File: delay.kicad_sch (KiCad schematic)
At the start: 50 parts, among them U1 L7805, U2 TL072, U3 PT2399

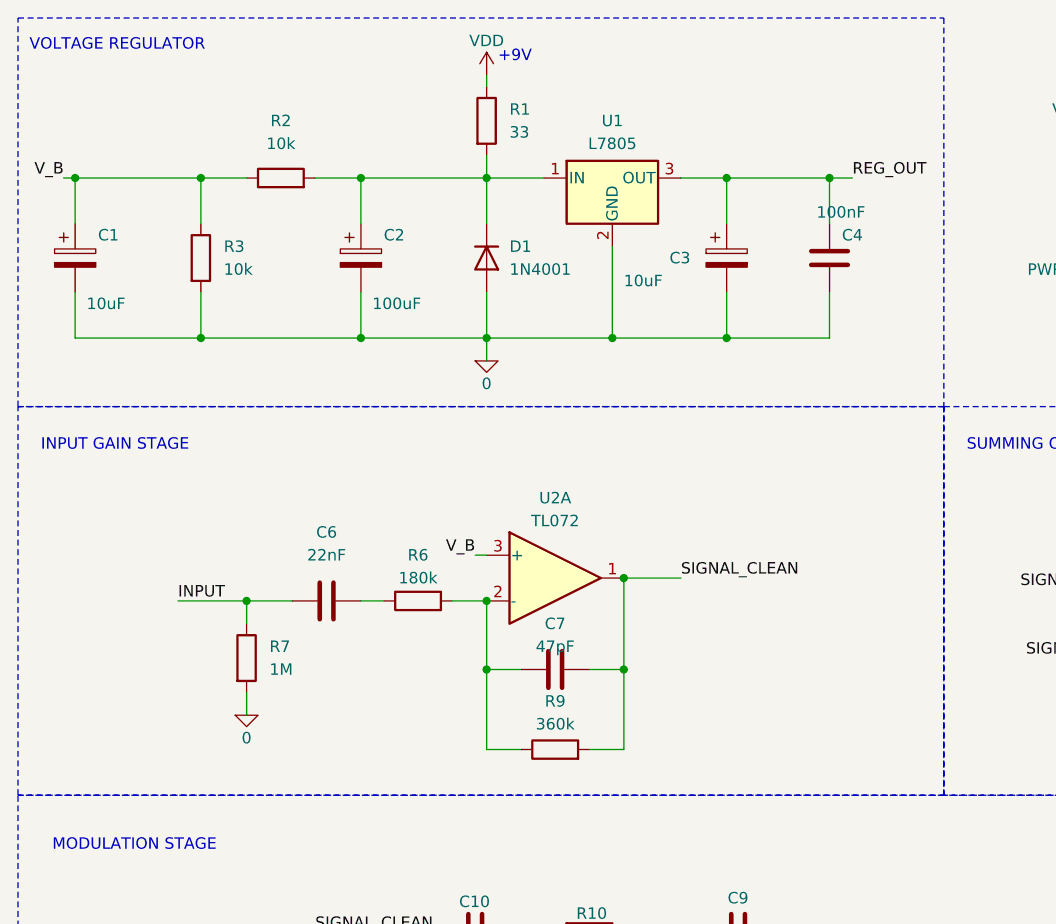
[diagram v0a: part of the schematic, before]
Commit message: add footprint for each element
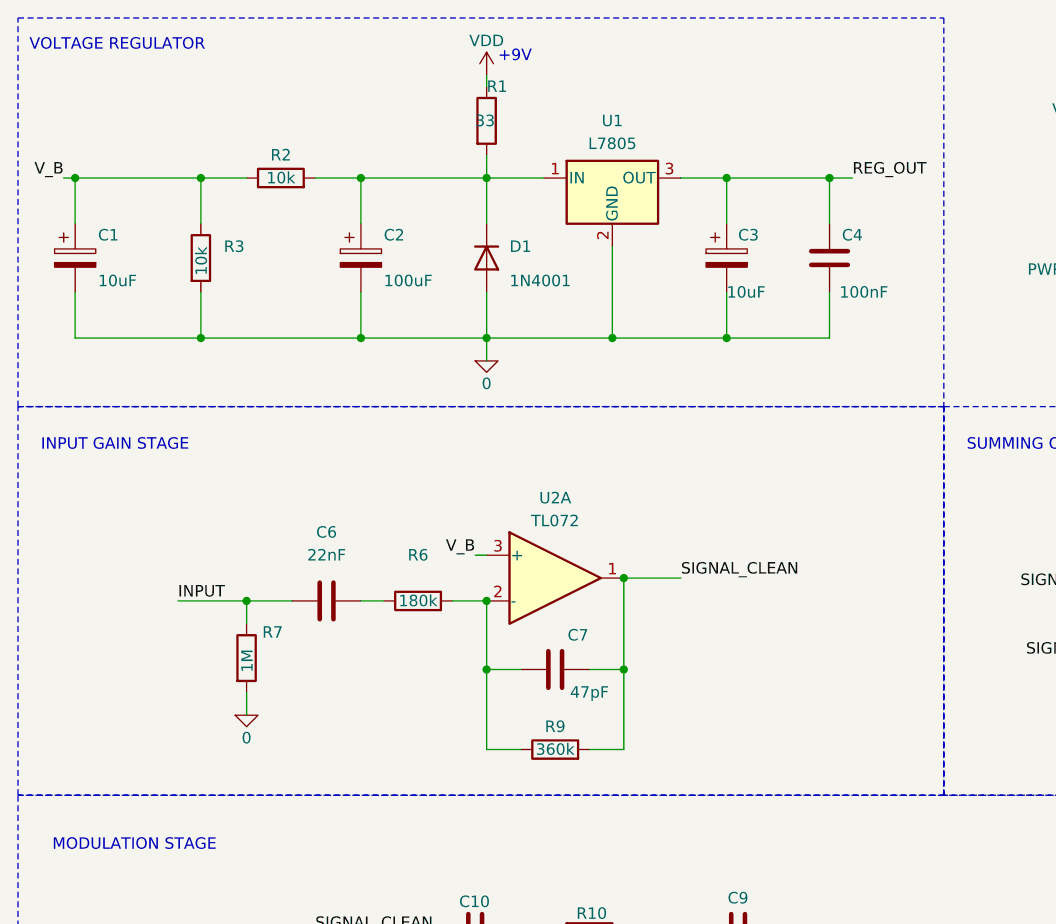
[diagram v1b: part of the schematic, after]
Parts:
- C1, C13, C2, C3: footprint (none) -> Capacitor_SMD:CP_Elec_8x10
- C10, C11, C12, C14, C15, C16, C17, C18, C19, C20, C21, C22, C23, C4, C5, C6, C7, C8, C9: footprint (none) -> Capacitor_SMD:C_0805_2012Metric_Pad1.18x1.45mm_HandSolder
- DELAY1, FDBK1, MIX1: footprint (none) -> Potentiometer_THT:Potentiometer_Alps_RK163_Single_Horizontal
- R1, R10, R11, R12, R13, R14, R15, R16, R17, R18, R19, R2, R20, R3, R4, R5, R6, R7, R8, R9: footprint (none) -> Resistor_SMD:R_0805_2012Metric_Pad1.20x1.40mm_HandSolder
- U1: footprint (none) -> Regulators:TO255P1020X450X2000-3
- U2: footprint (none) -> Op-Amps:DIP794W45P254L1060H508Q8

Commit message: add list of components and respective links, add real footprints
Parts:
- C1, C3: footprint Capacitor_SMD:CP_Elec_8x10 -> Capacitor:EEE1AA220WR
- C13, C2: footprint Capacitor_SMD:CP_Elec_8x10 -> Capacitor:EEE1AA101SP
- D1: footprint Diode_THT:D_DO-41_SOD81_P10.16mm_Horizontal -> Diodes:DIOM5226X240N
- U1: footprint Regulators:TO255P1020X450X2000-3 -> Ic:TO255P460X1020X2008-3P
- U2: footprint Op-Amps:DIP794W45P254L1060H508Q8 -> Ic:SOT65P280X110-8N
- U3: footprint Package_DIP:DIP-16_W7.62mm -> Package_SO:SOIC-16_3.9x9.9mm_P1.27mm
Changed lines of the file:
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@@
       (effects (font (size 1.27 1.27)) (justify left))
     )
-    (property "Footprint" "Capacitor_SMD:CP_Elec_8x10" (at 96.2152 44.45 0)
+    (property "Footprint" "Capacitor:EEE1AA220WR" (at 96.2152 44.45 0)
       (effects (font (size 1.27 1.27)) hide)
     )
@@
       (effects (font (size 1.27 1.27)))
     )
-    (property "Footprint" "Regulators:TO255P1020X450X2000-3" (at 83.185 35.56 0)
+    (property "Footprint" "Ic:TO255P460X1020X2008-3P" (at 83.185 35.56 0)
       (effects (font (size 1.27 1.27) italic) (justify left) hide)
     )
@@
       (effects (font (size 1.27 1.27)) (justify right))
     )
-    (property "Footprint" "Package_DIP:DIP-16_W7.62mm" (at 54.61 152.4 0)
+    (property "Footprint" "Package_SO:SOIC-16_3.9x9.9mm_P1.27mm" (at 54.61 152.4 0)
       (effects (font (size 1.27 1.27)) hide)
     )
@@
       (effects (font (size 1.27 1.27)))
     )
-    (property "Footprint" "Op-Amps:DIP794W45P254L1060H508Q8" (at 167.64 74.93 0)
+    (property "Footprint" "Ic:SOT65P280X110-8N" (at 167.64 74.93 0)
       (effects (font (size 1.27 1.27)) hide)
     )
@@
       (effects (font (size 1.27 1.27)) (justify left))
     )
-    (property "Footprint" "Diode_THT:D_DO-41_SOD81_P10.16mm_Horizontal" (at 68.58 40.64 0)
+    (property "Footprint" "Diodes:DIOM5226X240N" (at 68.58 40.64 0)
       (effects (font (size 1.27 1.27)) hide)
     )
@@
       (effects (font (size 1.27 1.27)))
     )
-    (property "Footprint" "Op-Amps:DIP794W45P254L1060H508Q8" (at 76.2 76.2 0)
+    (property "Footprint" "Ic:SOT65P280X110-8N" (at 76.2 76.2 0)
       (effects (font (size 1.27 1.27)) hide)
     )
@@
       (effects (font (size 1.27 1.27)) (justify left))
     )
-    (property "Footprint" "Capacitor_SMD:CP_Elec_8x10" (at 23.8252 44.45 0)
+    (property "Footprint" "Capacitor:EEE1AA220WR" (at 23.8252 44.45 0)
       (effects (font (size 1.27 1.27)) hide)
     )
@@
       (effects (font (size 1.27 1.27)) (justify left))
     )
-    (property "Footprint" "Capacitor_SMD:CP_Elec_8x10" (at 31.75 130.5052 0)
+    (property "Footprint" "Capacitor:EEE1AA101SP" (at 31.75 130.5052 0)
       (effects (font (size 1.27 1.27)) hide)
     )
@@
       (effects (font (size 1.27 1.27)) (justify left))
     )
-    (property "Footprint" "Capacitor_SMD:CP_Elec_8x10" (at 55.5752 44.45 0)
-      (effects (font (size 1.27 1.27)) hide)
-    )
+    (property "Footprint" "Capacitor:EEE1AA101SP" (at 55.5752 44.45 0)
+      (effects (font (size 1.27 1.27)) hide)
+    )

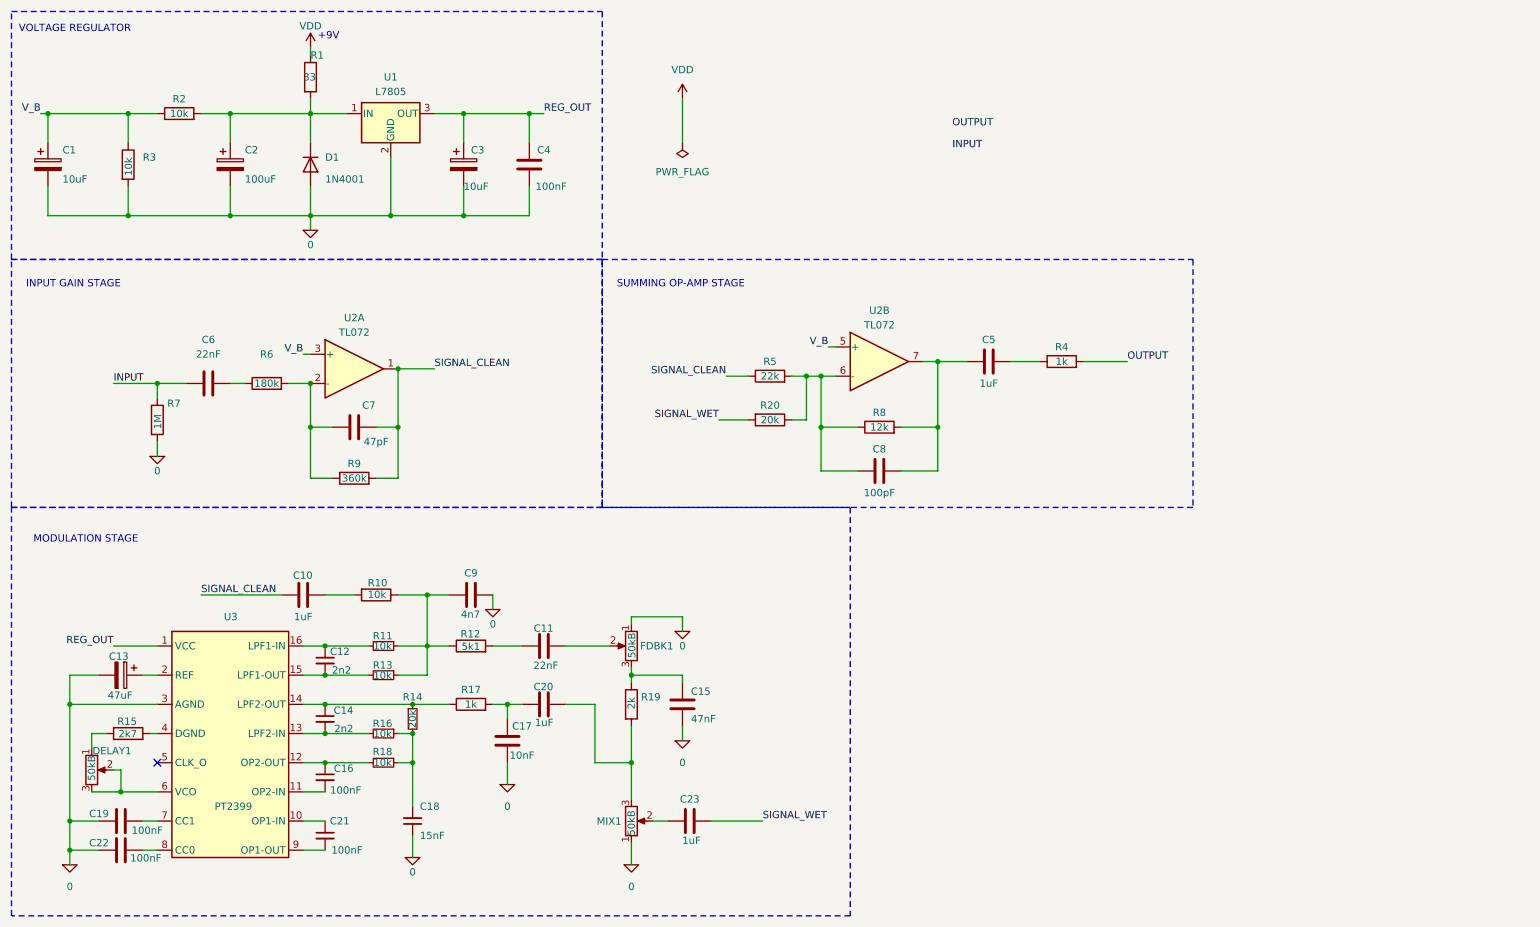
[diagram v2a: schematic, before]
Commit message: add screw connectors
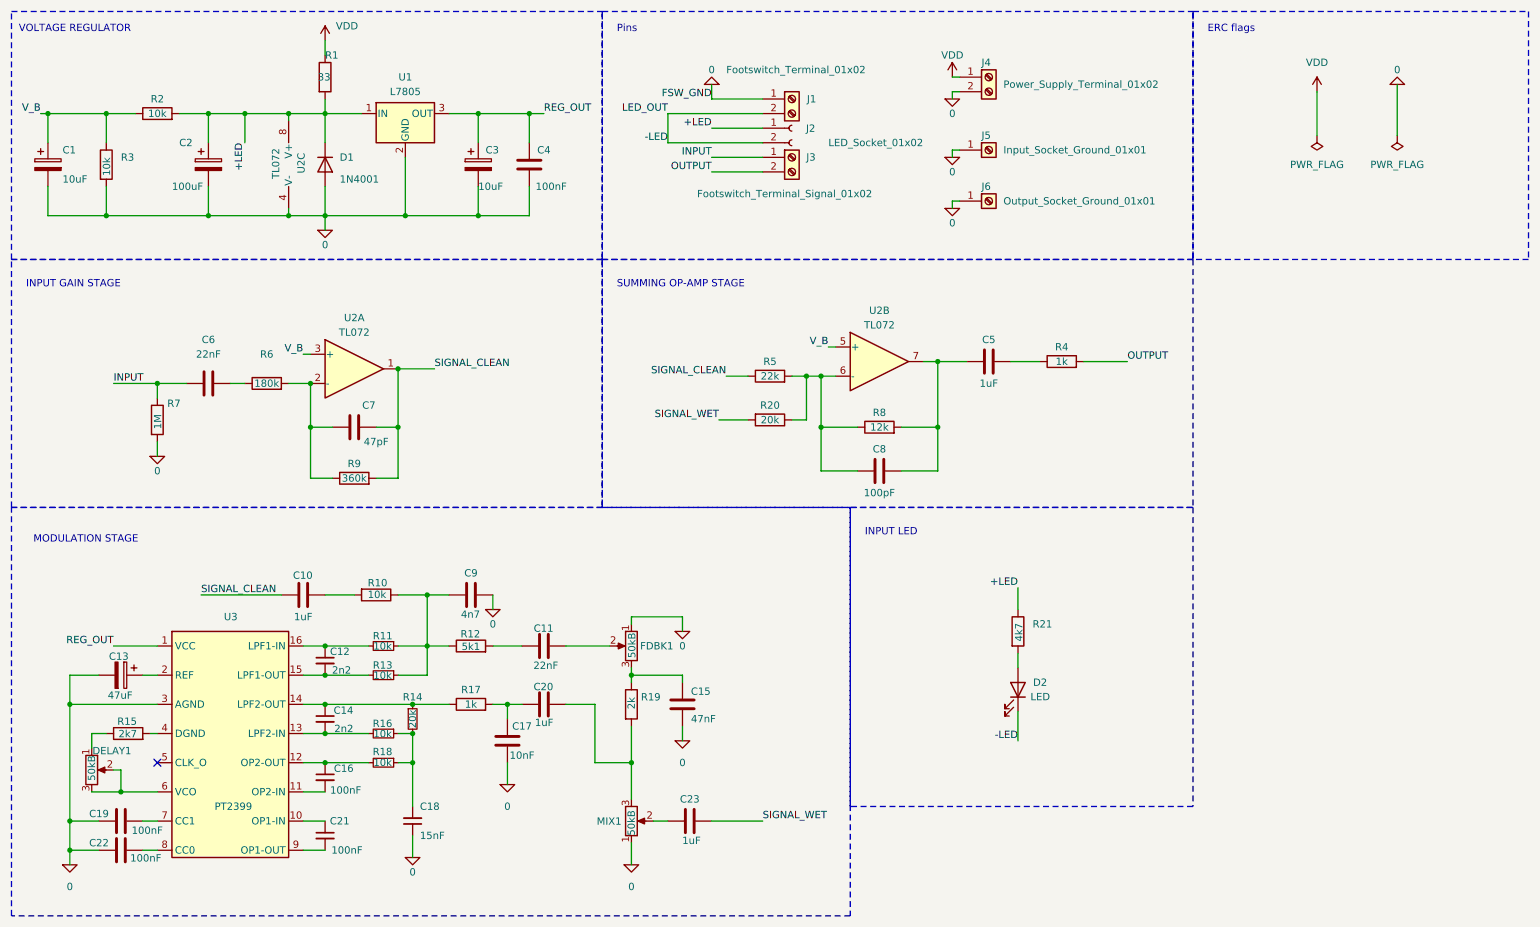
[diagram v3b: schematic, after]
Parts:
- added D2: LED, symbol Device:LED
- added J1: Footswitch_Terminal_01x02, symbol Connector:Screw_Terminal_01x02
- added J2: LED_Socket_01x02, symbol Connector:Conn_01x02_Socket
- added J3: Footswitch_Terminal_Signal_01x02, symbol Connector:Screw_Terminal_01x02
- added J4: Power_Supply_Terminal_01x02, symbol Connector:Screw_Terminal_01x02
- added J5: Input_Socket_Ground_01x01, symbol Connector:Screw_Terminal_01x01
- added J6: Output_Socket_Ground_01x01, symbol Connector:Screw_Terminal_01x01
- added R21: 4k7, symbol Device:R
- added unit 3 of U2
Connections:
- net 0: now also J1.1 (Pin_1), J4.2 (Pin_2), J5.1 (Pin_1), J6.1 (Pin_1), U2.4 (V-)
- net INPUT: now also J3.1 (Pin_1)
- net OUTPUT: now also J3.2 (Pin_2)
- net VDD: now also J4.1 (Pin_1)
- net +LED: now reaches C2.1, D1.1 (K), R1.2, R2.2, U1.1 (IN)
- net +LED: now also J2.1 (Pin_1), R21.1, U2.8 (V+)
- new net: D2.2 (A), R21.2
- new net -LED: D2.1 (K), J1.2 (Pin_2), J2.2 (Pin_2)
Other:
- note added: "ERC flags"
- note added: "INPUT LED"
- note added: "Pins"
- note removed: "+9V"
- moved on the sheet: C2, C3, D1, R1, R2, R3, U1

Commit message: update design rules for pcb creator to match requirements
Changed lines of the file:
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@@
+    (stroke (width 0) (type default))
+  )
+  (wire (pts (xy 180.34 20.32) (xy 180.34 25.4))
     (stroke (width 0) (type default))
   )
@@
     (stroke (width 0) (type default))
   )
+  (wire (pts (xy 180.34 25.4) (xy 181.61 25.4))
+    (stroke (width 0) (type default))
+  )
   (wire (pts (xy 67.31 73.66) (xy 68.58 73.66))
     (stroke (width 0) (type default))
@@
   )
   (wire (pts (xy 26.67 134.62) (xy 26.67 154.94))
-    (stroke (width 0) (type default))
-  )
-  (wire (pts (xy 180.34 25.4) (xy 181.61 25.4))
     (stroke (width 0) (type default))
   )
@@
     (effects (font (size 1.27 1.27)) (justify left bottom))
   )
+  (label "+9V" (at 71.12 20.32 0) (fields_autoplaced)
+    (effects (font (size 1.27 1.27)) (justify left bottom))
+  )
   (label "SIGNAL_WET" (at 139.7 85.09 180) (fields_autoplaced)
     (effects (font (size 1.27 1.27)) (justify right bottom))
@@
   (label "LED_OUT" (at 130.81 31.75 180) (fields_autoplaced)
     (effects (font (size 1.27 1.27)) (justify right bottom))
+  )
+  (label "+9V" (at 180.34 21.59 0) (fields_autoplaced)
+    (effects (font (size 1.27 1.27)) (justify left bottom))
   )
   (label "+LED" (at 57.15 36.83 270) (fields_autoplaced)
@@
     )
   )
-  (symbol (lib_id "power:VDD") (at 180.34 25.4 0) (unit 1)
-    (in_bom yes) (on_board yes) (dnp no)
-    (property "Reference" "#PWR03" (at 180.34 29.21 0)
-      (effects (font (size 1.27 1.27)) hide)
-    )
-    (property "Value" "VDD" (at 180.34 21.59 0)
-      (effects (font (size 1.27 1.27)))
-    )
-    (property "Footprint" "" (at 180.34 25.4 0)
-      (effects (font (size 1.27 1.27)) hide)
-    )
-    (property "Datasheet" "" (at 180.34 25.4 0)
-      (effects (font (size 1.27 1.27)) hide)
-    )
+  (symbol (lib_id "power:VDD") (at 180.34 20.32 0) (unit 1)
+    (in_bom yes) (on_board yes) (dnp no)
+    (property "Reference" "#PWR03" (at 180.34 24.13 0)
+      (effects (font (size 1.27 1.27)) hide)
+    )
+    (property "Value" "VDD" (at 180.34 16.51 0)
+      (effects (font (size 1.27 1.27)))
+    )
+    (property "Footprint" "" (at 180.34 20.32 0)
+      (effects (font (size 1.27 1.27)) hide)
+    )
+    (property "Datasheet" "" (at 180.34 20.32 0)
+      (effects (font (size 1.27 1.27)) hide)
+    )

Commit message: add remaining footprints, start pcb design process
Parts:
- removed J5: Input_Socket_Ground_01x01, symbol Connector:Screw_Terminal_01x01
- removed J6: Output_Socket_Ground_01x01, symbol Connector:Screw_Terminal_01x01
- added J5: IO_Ground_Terminal_01x02, Terminal:TB00150002BE, symbol Connector:Screw_Terminal_01x02
- D2, J2: footprint (none) -> Diodes:TB00150002BE
- J1, J3, J4: footprint (none) -> Terminal:TB00150002BE
- R21: footprint (none) -> Resistor_SMD:R_0805_2012Metric_Pad1.20x1.40mm_HandSolder
- U2: footprint (none) -> Ic:SOT65P280X110-8N
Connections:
- net 0: now also J5.1 (Pin_1), J5.2 (Pin_2)
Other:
- moved on the sheet: J2
